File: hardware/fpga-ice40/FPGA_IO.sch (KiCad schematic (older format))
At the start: 1 part, among them U1 iCE40HX4K-TQ144

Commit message: Component selection by MPN and routing cleanup
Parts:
- U1: MPN (none) -> iCE40HX4K-TQ144; manf# iCE40HX4K-TQ144 -> (none)
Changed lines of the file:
@@
 F 2 "Package_QFP:TQFP-144_20x20mm_P0.5mm" H 7850 2900 60  0001 L CNN
 F 3 "https://www.mouser.com/datasheet/2/225/FPGA-DS-02029-3-5-iCE40-LP-HX-Family-Data-Sheet-1022803.pdf" H 7850 2700 60  0001 L CNN
-F 4 "iCE40HX4K-TQ144" H 7850 2800 60  0001 L CNN "manf#"
+F 4 "" H 7850 2800 60  0001 L CNN "manf#"
+F 5 "iCE40HX4K-TQ144" H 7650 2850 50  0001 C CNN "MPN"
 	4    7650 2850
 	1    0    0    -1
@@
 F 2 "Package_QFP:TQFP-144_20x20mm_P0.5mm" H 5850 2900 60  0001 L CNN
 F 3 "https://www.mouser.com/datasheet/2/225/FPGA-DS-02029-3-5-iCE40-LP-HX-Family-Data-Sheet-1022803.pdf" H 5850 2700 60  0001 L CNN
-F 4 "iCE40HX4K-TQ144" H 5850 2800 60  0001 L CNN "manf#"
+F 4 "" H 5850 2800 60  0001 L CNN "manf#"
+F 5 "iCE40HX4K-TQ144" H 5650 2850 50  0001 C CNN "MPN"
 	3    5650 2850
 	1    0    0    -1
@@
 F 2 "Package_QFP:TQFP-144_20x20mm_P0.5mm" H 3850 2850 60  0001 L CNN
 F 3 "https://www.mouser.com/datasheet/2/225/FPGA-DS-02029-3-5-iCE40-LP-HX-Family-Data-Sheet-1022803.pdf" H 3850 2650 60  0001 L CNN
-F 4 "iCE40HX4K-TQ144" H 3850 2750 60  0001 L CNN "manf#"
+F 4 "" H 3850 2750 60  0001 L CNN "manf#"
+F 5 "iCE40HX4K-TQ144" H 3650 2800 50  0001 C CNN "MPN"
 	2    3650 2800
 	1    0    0    -1
@@
 F 2 "Package_QFP:TQFP-144_20x20mm_P0.5mm" H 1850 2900 60  0001 L CNN
 F 3 "https://www.mouser.com/datasheet/2/225/FPGA-DS-02029-3-5-iCE40-LP-HX-Family-Data-Sheet-1022803.pdf" H 1850 2700 60  0001 L CNN
-F 4 "iCE40HX4K-TQ144" H 1850 2800 60  0001 L CNN "manf#"
+F 4 "iCE40HX4K-TQ144" H 1650 2850 50  0001 C CNN "MPN"
 	1    1650 2850
 	1    0    0    -1

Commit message: Completed verification of all pins for all symbols
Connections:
- net SD_CD renamed SD_DET
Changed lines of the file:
@@
 LED_D0
 Text GLabel 4850 3400 2    50   Input ~ 0
-SD_CD
+SD_DET
 Text GLabel 4850 3300 2    50   Input ~ 0
 SD_DAT2

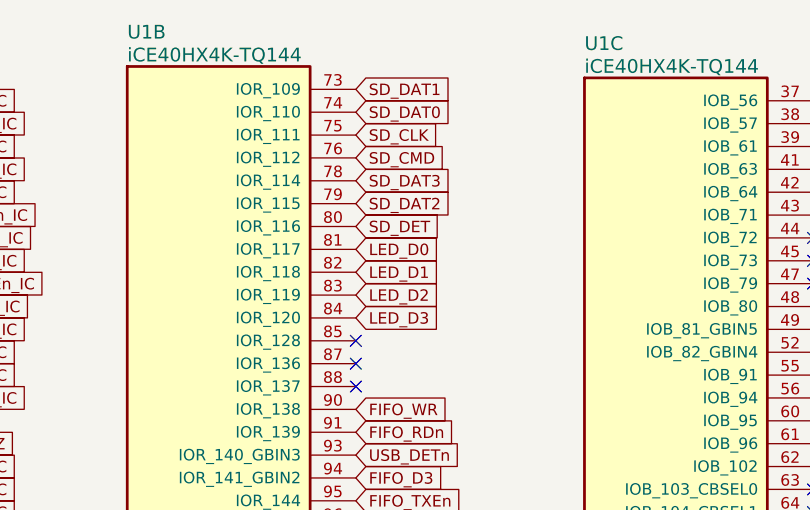
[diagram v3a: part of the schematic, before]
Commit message: Rename SD_DET signal to SD_CD for consistency
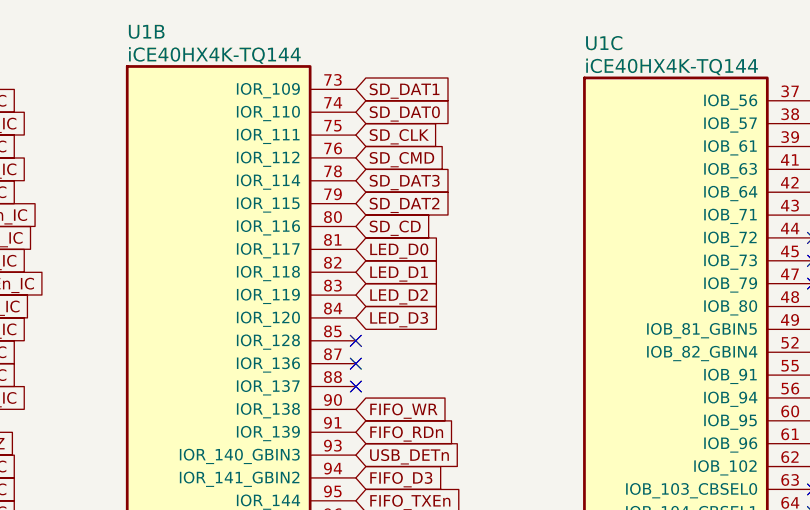
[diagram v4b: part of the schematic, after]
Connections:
- net SD_DET renamed SD_CD
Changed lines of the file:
@@
 LED_D0
 Text GLabel 4850 3400 2    50   Input ~ 0
-SD_DET
+SD_CD
 Text GLabel 4850 3300 2    50   Input ~ 0
 SD_DAT2

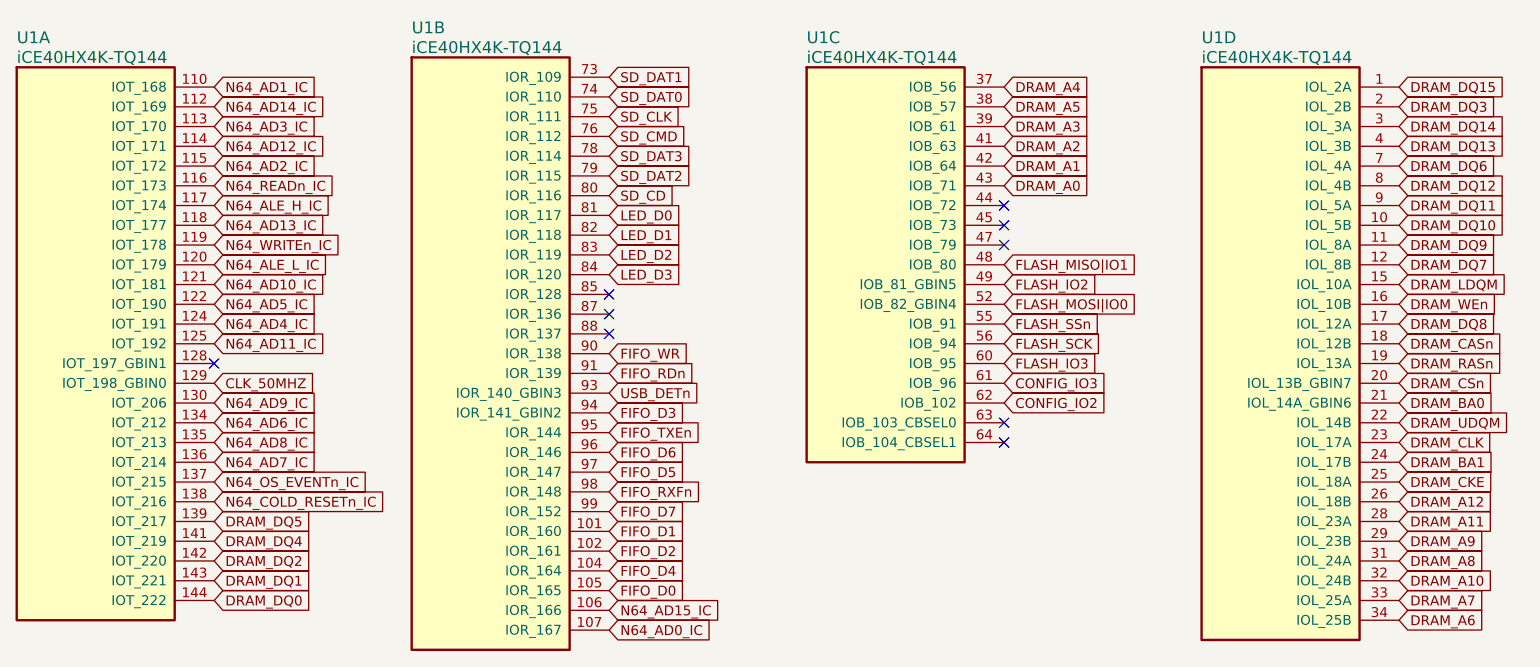
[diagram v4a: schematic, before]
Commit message: Fix mechanical issue by moving USB connector to top of board
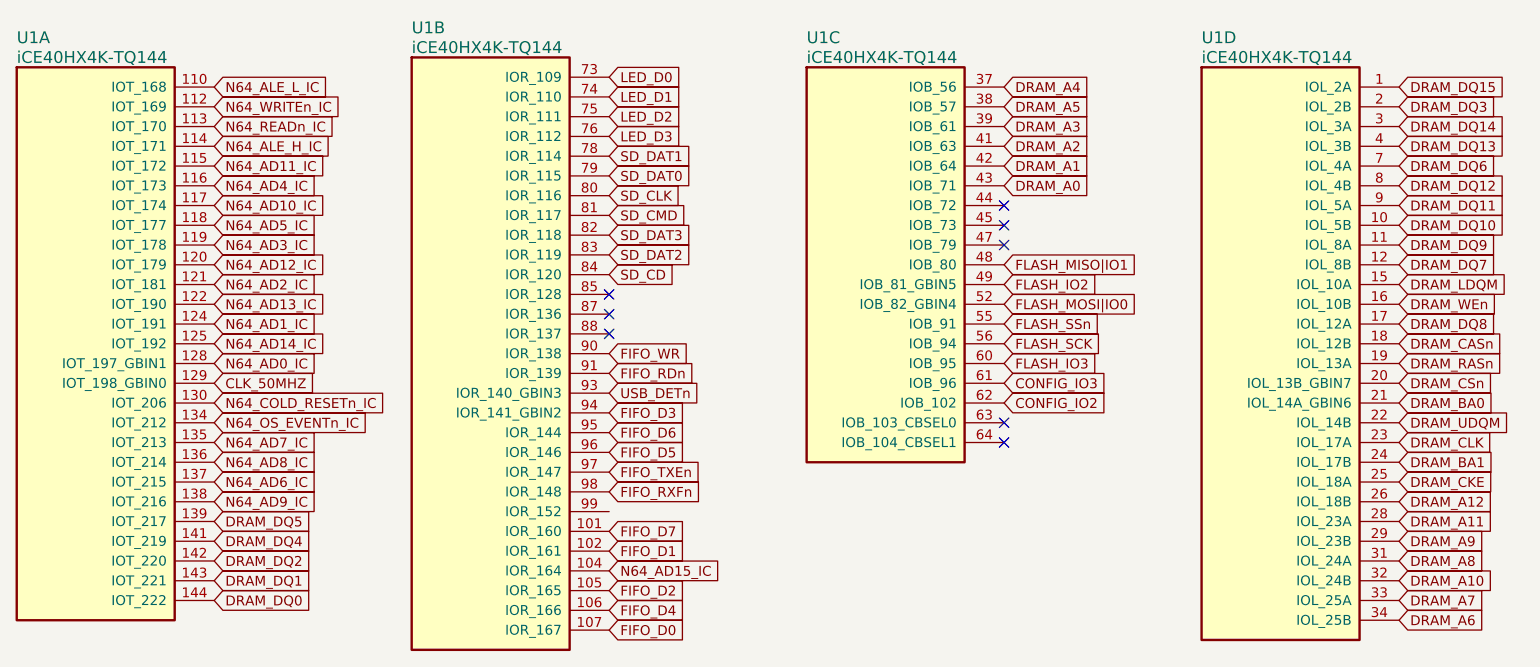
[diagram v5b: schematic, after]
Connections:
- net FIFO_D0: now also U1.107 (IOR_167); no longer U1.105 (IOR_165)
- net FIFO_D1: now also U1.102 (IOR_161); no longer U1.101 (IOR_160)
- net FIFO_D2: now also U1.105 (IOR_165); no longer U1.102 (IOR_161)
- net FIFO_D4: now also U1.106 (IOR_166); no longer U1.104 (IOR_164)
- net FIFO_D5: now also U1.96 (IOR_146); no longer U1.97 (IOR_147)
- net FIFO_D6: now also U1.95 (IOR_144); no longer U1.96 (IOR_146)
- net FIFO_D7: now also U1.101 (IOR_160); no longer U1.99 (IOR_152)
- net FIFO_TXEn: now also U1.97 (IOR_147); no longer U1.95 (IOR_144)
- net LED_D0: now also U1.73 (IOR_109); no longer U1.81 (IOR_117)
- net LED_D1: now also U1.74 (IOR_110); no longer U1.82 (IOR_118)
- net LED_D2: now also U1.75 (IOR_111); no longer U1.83 (IOR_119)
- net LED_D3: now also U1.76 (IOR_112); no longer U1.84 (IOR_120)
- net N64_AD0_IC: now also U1.128 (IOT_197_GBIN1); no longer U1.107 (IOR_167)
- net N64_AD10_IC: now also U1.117 (IOT_174); no longer U1.121 (IOT_181)
- net N64_AD11_IC: now also U1.115 (IOT_172); no longer U1.125 (IOT_192)
- net N64_AD12_IC: now also U1.120 (IOT_179); no longer U1.114 (IOT_171)
- net N64_AD13_IC: now also U1.122 (IOT_190); no longer U1.118 (IOT_177)
- net N64_AD14_IC: now also U1.125 (IOT_192); no longer U1.112 (IOT_169)
- net N64_AD15_IC: now also U1.104 (IOR_164); no longer U1.106 (IOR_166)
- net N64_AD1_IC: now also U1.124 (IOT_191); no longer U1.110 (IOT_168)
- net N64_AD2_IC: now also U1.121 (IOT_181); no longer U1.115 (IOT_172)
- net N64_AD3_IC: now also U1.119 (IOT_178); no longer U1.113 (IOT_170)
- net N64_AD4_IC: now also U1.116 (IOT_173); no longer U1.124 (IOT_191)
- net N64_AD5_IC: now also U1.118 (IOT_177); no longer U1.122 (IOT_190)
- net N64_AD6_IC: now also U1.137 (IOT_215); no longer U1.134 (IOT_212)
- net N64_AD7_IC: now also U1.135 (IOT_213); no longer U1.136 (IOT_214)
- net N64_AD8_IC: now also U1.136 (IOT_214); no longer U1.135 (IOT_213)
- net N64_AD9_IC: now also U1.138 (IOT_216); no longer U1.130 (IOT_206)
- net N64_ALE_H_IC: now also U1.114 (IOT_171); no longer U1.117 (IOT_174)
- net N64_ALE_L_IC: now also U1.110 (IOT_168); no longer U1.120 (IOT_179)
- net N64_COLD_RESETn_IC: now also U1.130 (IOT_206); no longer U1.138 (IOT_216)
- net N64_OS_EVENTn_IC: now also U1.134 (IOT_212); no longer U1.137 (IOT_215)
- net N64_READn_IC: now also U1.113 (IOT_170); no longer U1.116 (IOT_173)
- net N64_WRITEn_IC: now also U1.112 (IOT_169); no longer U1.119 (IOT_178)
- net SD_CD: now also U1.84 (IOR_120); no longer U1.80 (IOR_116)
- net SD_CLK: now also U1.80 (IOR_116); no longer U1.75 (IOR_111)
- net SD_CMD: now also U1.81 (IOR_117); no longer U1.76 (IOR_112)
- net SD_DAT0: now also U1.79 (IOR_115); no longer U1.74 (IOR_110)
- net SD_DAT1: now also U1.78 (IOR_114); no longer U1.73 (IOR_109)
- net SD_DAT2: now also U1.83 (IOR_119); no longer U1.79 (IOR_115)
- net SD_DAT3: now also U1.82 (IOR_118); no longer U1.78 (IOR_114)
- no-connect marks 9 -> 8
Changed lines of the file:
@@
 NoConn ~ 4850 4000
 NoConn ~ 4850 3900
-NoConn ~ 2850 4250
 Text GLabel 2850 4350 2    50   Input ~ 0
 CLK_50MHZ
+Text GLabel 4850 3100 2    50   Input ~ 0
+LED_D3
+Text GLabel 4850 3000 2    50   Input ~ 0
+LED_D2
+Text GLabel 4850 2900 2    50   Input ~ 0
+LED_D1
+Text GLabel 4850 2800 2    50   Input ~ 0
+LED_D0
 Text GLabel 4850 3800 2    50   Input ~ 0
-LED_D3
+SD_CD
 Text GLabel 4850 3700 2    50   Input ~ 0
-LED_D2
+SD_DAT2
 Text GLabel 4850 3600 2    50   Input ~ 0
-LED_D1
+SD_DAT3
 Text GLabel 4850 3500 2    50   Input ~ 0
-LED_D0
+SD_CMD
+Text GLabel 4850 3200 2    50   Input ~ 0
+SD_DAT1
+Text GLabel 4850 3300 2    50   Input ~ 0
+SD_DAT0
 Text GLabel 4850 3400 2    50   Input ~ 0
-SD_CD
-Text GLabel 4850 3300 2    50   Input ~ 0
-SD_DAT2
-Text GLabel 4850 3200 2    50   Input ~ 0
-SD_DAT3
-Text GLabel 4850 3100 2    50   Input ~ 0
-SD_CMD
-Text GLabel 4850 2800 2    50   Input ~ 0
-SD_DAT1
-Text GLabel 4850 2900 2    50   Input ~ 0
-SD_DAT0
-Text GLabel 4850 3000 2    50   Input ~ 0
 SD_CLK
 Text GLabel 8850 5350 2    50   Input ~ 0
@@
 Text GLabel 4850 4400 2    50   Input ~ 0
 USB_DETn
-Text GLabel 4850 4600 2    50   Input ~ 0
+Text GLabel 4850 4800 2    50   Input ~ 0
 FIFO_TXEn
 Text GLabel 4850 4200 2    50   Input ~ 0
@@
 Text GLabel 4850 4900 2    50   Input ~ 0
 FIFO_RXFn
-Text GLabel 4850 4800 2    50   Input ~ 0
+Text GLabel 4850 4700 2    50   Input ~ 0
 FIFO_D5
-Text GLabel 4850 5000 2    50   Input ~ 0
+Text GLabel 4850 5100 2    50   Input ~ 0
 FIFO_D7
-Text GLabel 4850 4700 2    50   Input ~ 0
+Text GLabel 4850 4600 2    50   Input ~ 0
 FIFO_D6
-Text GLabel 4850 5300 2    50   Input ~ 0
+Text GLabel 4850 5500 2    50   Input ~ 0
 FIFO_D4
 Text GLabel 4850 4500 2    50   Input ~ 0
 FIFO_D3
+Text GLabel 4850 5400 2    50   Input ~ 0
+FIFO_D2
 Text GLabel 4850 5200 2    50   Input ~ 0
-FIFO_D2
-Text GLabel 4850 5100 2    50   Input ~ 0
 FIFO_D1
-Text GLabel 4850 5400 2    50   Input ~ 0
+Text GLabel 4850 5600 2    50   Input ~ 0
 FIFO_D0
 Text GLabel 6850 2950 2    50   Input ~ 0
@@
 Text GLabel 8850 4050 2    50   Input ~ 0
 DRAM_DQ8
+Text GLabel 2850 4650 2    50   Input ~ 0
+N64_AD7_IC
+Text GLabel 2850 4850 2    50   Input ~ 0
+N64_AD6_IC
+Text GLabel 2850 3550 2    50   Input ~ 0
+N64_AD5_IC
+Text GLabel 2850 3350 2    50   Input ~ 0
+N64_AD4_IC
+Text GLabel 2850 4550 2    50   Input ~ 0
+N64_OS_EVENTn_IC
+Text GLabel 2850 4450 2    50   Input ~ 0
+N64_COLD_RESETn_IC
 Text GLabel 2850 4750 2    50   Input ~ 0
-N64_AD7_IC
-Text GLabel 2850 4550 2    50   Input ~ 0
-N64_AD6_IC
+N64_AD8_IC
+Text GLabel 2850 4950 2    50   Input ~ 0
+N64_AD9_IC
+Text GLabel 2850 3450 2    50   Input ~ 0
+N64_AD10_IC
+Text GLabel 2850 3250 2    50   Input ~ 0
+N64_AD11_IC
+Text GLabel 2850 3750 2    50   Input ~ 0
+N64_AD12_IC
 Text GLabel 2850 3950 2    50   Input ~ 0
-N64_AD5_IC
-Text GLabel 2850 4050 2    50   Input ~ 0
-N64_AD4_IC
-Text GLabel 2850 4850 2    50   Input ~ 0
-N64_OS_EVENTn_IC
-Text GLabel 2850 4950 2    50   Input ~ 0
-N64_COLD_RESETn_IC
-Text GLabel 2850 4650 2    50   Input ~ 0
-N64_AD8_IC
-Text GLabel 2850 4450 2    50   Input ~ 0
-N64_AD9_IC
+N64_AD13_IC
+Text GLabel 2850 3050 2    50   Input ~ 0
+N64_READn_IC
+Text GLabel 2850 2950 2    50   Input ~ 0
+N64_WRITEn_IC
+Text GLabel 2850 3150 2    50   Input ~ 0
+N64_ALE_H_IC
+Text GLabel 2850 2850 2    50   Input ~ 0
+N64_ALE_L_IC
+Text GLabel 2850 3650 2    50   Input ~ 0
+N64_AD3_IC
 Text GLabel 2850 3850 2    50   Input ~ 0
-N64_AD10_IC
-Text GLabel 2850 4150 2    50   Input ~ 0
-N64_AD11_IC
-Text GLabel 2850 3150 2    50   Input ~ 0
-N64_AD12_IC
-Text GLabel 2850 3550 2    50   Input ~ 0
-N64_AD13_IC
-Text GLabel 2850 3350 2    50   Input ~ 0
-N64_READn_IC
-Text GLabel 2850 3650 2    50   Input ~ 0
-N64_WRITEn_IC
-Text GLabel 2850 3450 2    50   Input ~ 0
-N64_ALE_H_IC
-Text GLabel 2850 3750 2    50   Input ~ 0
-N64_ALE_L_IC
-Text GLabel 2850 3050 2    50   Input ~ 0
-N64_AD3_IC
-Text GLabel 2850 3250 2    50   Input ~ 0
 N64_AD2_IC
-Text GLabel 2850 2850 2    50   Input ~ 0
-N64_AD1_IC
-Text GLabel 2850 2950 2    50   Input ~ 0
-N64_AD14_IC
-Text GLabel 4850 5500 2    50   Input ~ 0
+Text GLabel 4850 5300 2    50   Input ~ 0
 N64_AD15_IC
-Text GLabel 4850 5600 2    50   Input ~ 0
+Text GLabel 2850 4250 2    50   Input ~ 0
 N64_AD0_IC
 Text GLabel 6850 4250 2    50   Input ~ 0
@@
 	1    0    0    -1
 $EndComp
+Text GLabel 2850 4150 2    50   Input ~ 0
+N64_AD14_IC
+Text GLabel 2850 4050 2    50   Input ~ 0
+N64_AD1_IC
 $EndSCHEMATC

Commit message: Continuing routing after replacement
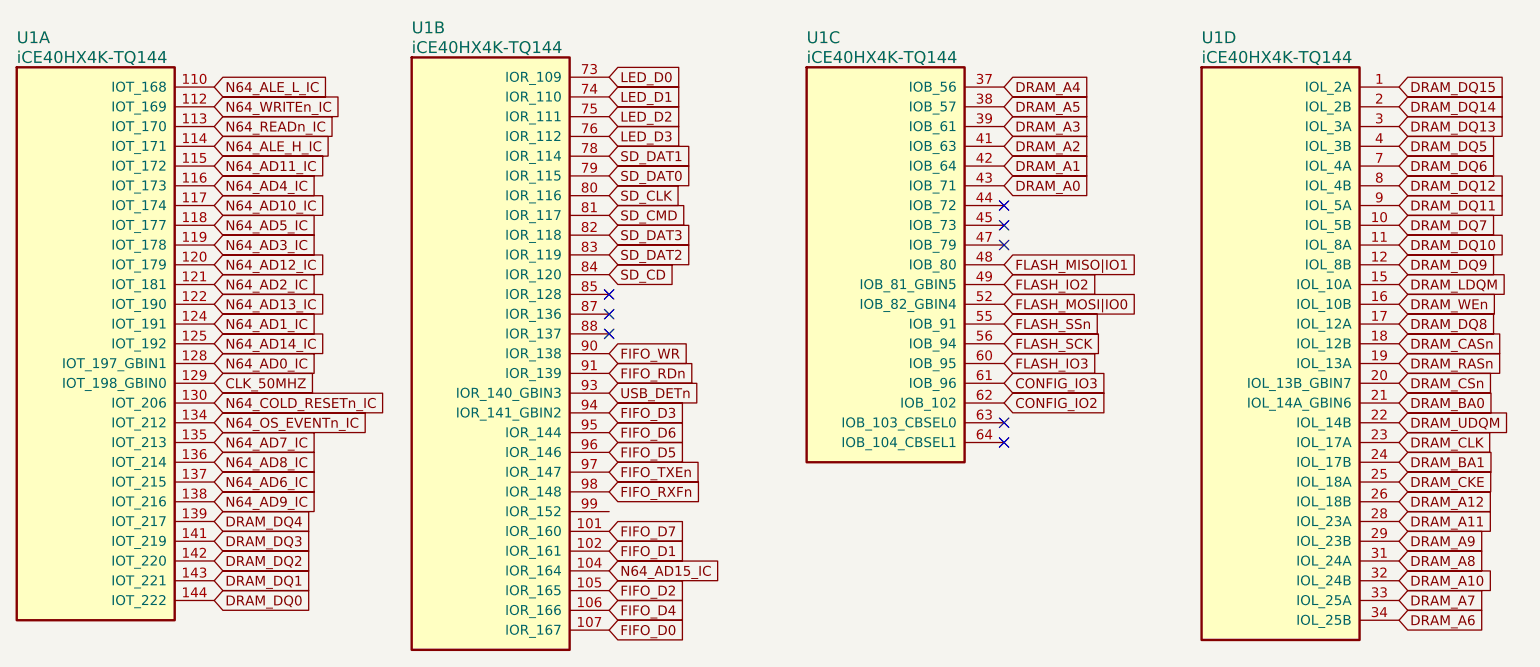
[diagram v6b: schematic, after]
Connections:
- net DRAM_DQ10: now also U1.11 (IOL_8A); no longer U1.10 (IOL_5B)
- net DRAM_DQ13: now also U1.3 (IOL_3A); no longer U1.4 (IOL_3B)
- net DRAM_DQ14: now also U1.2 (IOL_2B); no longer U1.3 (IOL_3A)
- net DRAM_DQ3: now also U1.141 (IOT_219); no longer U1.2 (IOL_2B)
- net DRAM_DQ4: now also U1.139 (IOT_217); no longer U1.141 (IOT_219)
- net DRAM_DQ5: now also U1.4 (IOL_3B); no longer U1.139 (IOT_217)
- net DRAM_DQ7: now also U1.10 (IOL_5B); no longer U1.12 (IOL_8B)
- net DRAM_DQ9: now also U1.12 (IOL_8B); no longer U1.11 (IOL_8A)
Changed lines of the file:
@@
 Text GLabel 6850 3350 2    50   Input ~ 0
 DRAM_A0
-Text GLabel 8850 3750 2    50   Input ~ 0
+Text GLabel 8850 3550 2    50   Input ~ 0
 DRAM_DQ7
 Text GLabel 8850 3250 2    50   Input ~ 0
 DRAM_DQ6
+Text GLabel 8850 3150 2    50   Input ~ 0
+DRAM_DQ5
 Text GLabel 2850 5050 2    50   Input ~ 0
-DRAM_DQ5
+DRAM_DQ4
 Text GLabel 2850 5150 2    50   Input ~ 0
-DRAM_DQ4
-Text GLabel 8850 2950 2    50   Input ~ 0
 DRAM_DQ3
 Text GLabel 2850 5250 2    50   Input ~ 0
@@
 Text GLabel 8850 2850 2    50   Input ~ 0
 DRAM_DQ15
+Text GLabel 8850 2950 2    50   Input ~ 0
+DRAM_DQ14
 Text GLabel 8850 3050 2    50   Input ~ 0
-DRAM_DQ14
-Text GLabel 8850 3150 2    50   Input ~ 0
 DRAM_DQ13
 Text GLabel 8850 3350 2    50   Input ~ 0
@@
 Text GLabel 8850 3450 2    50   Input ~ 0
 DRAM_DQ11
-Text GLabel 8850 3550 2    50   Input ~ 0
+Text GLabel 8850 3650 2    50   Input ~ 0
 DRAM_DQ10
-Text GLabel 8850 3650 2    50   Input ~ 0
+Text GLabel 8850 3750 2    50   Input ~ 0
 DRAM_DQ9
 Text GLabel 8850 4050 2    50   Input ~ 0
